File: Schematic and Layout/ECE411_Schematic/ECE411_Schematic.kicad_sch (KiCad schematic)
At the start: 17 parts, among them J1 Raspberry Pi GPIO, J2 AudioJack3, M1 Motor_DC, U1 CAT24C256, U2 PCF8574, U3 LM386, U4 L293D Driver

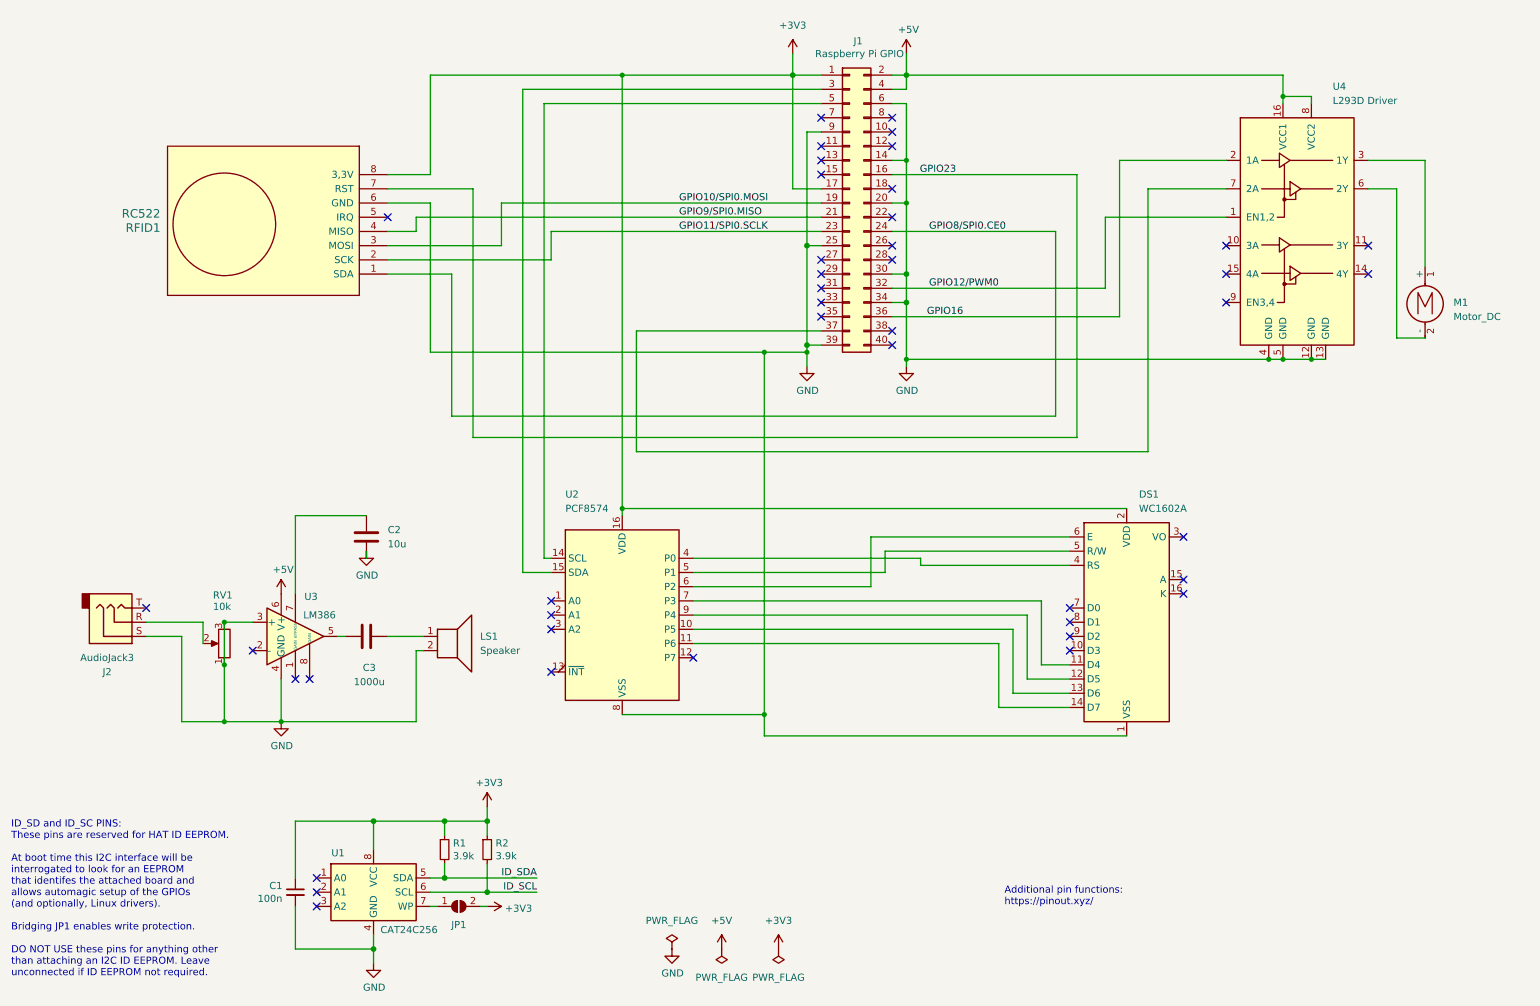
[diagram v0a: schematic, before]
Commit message: added LEDs to indicate functioning subsystems
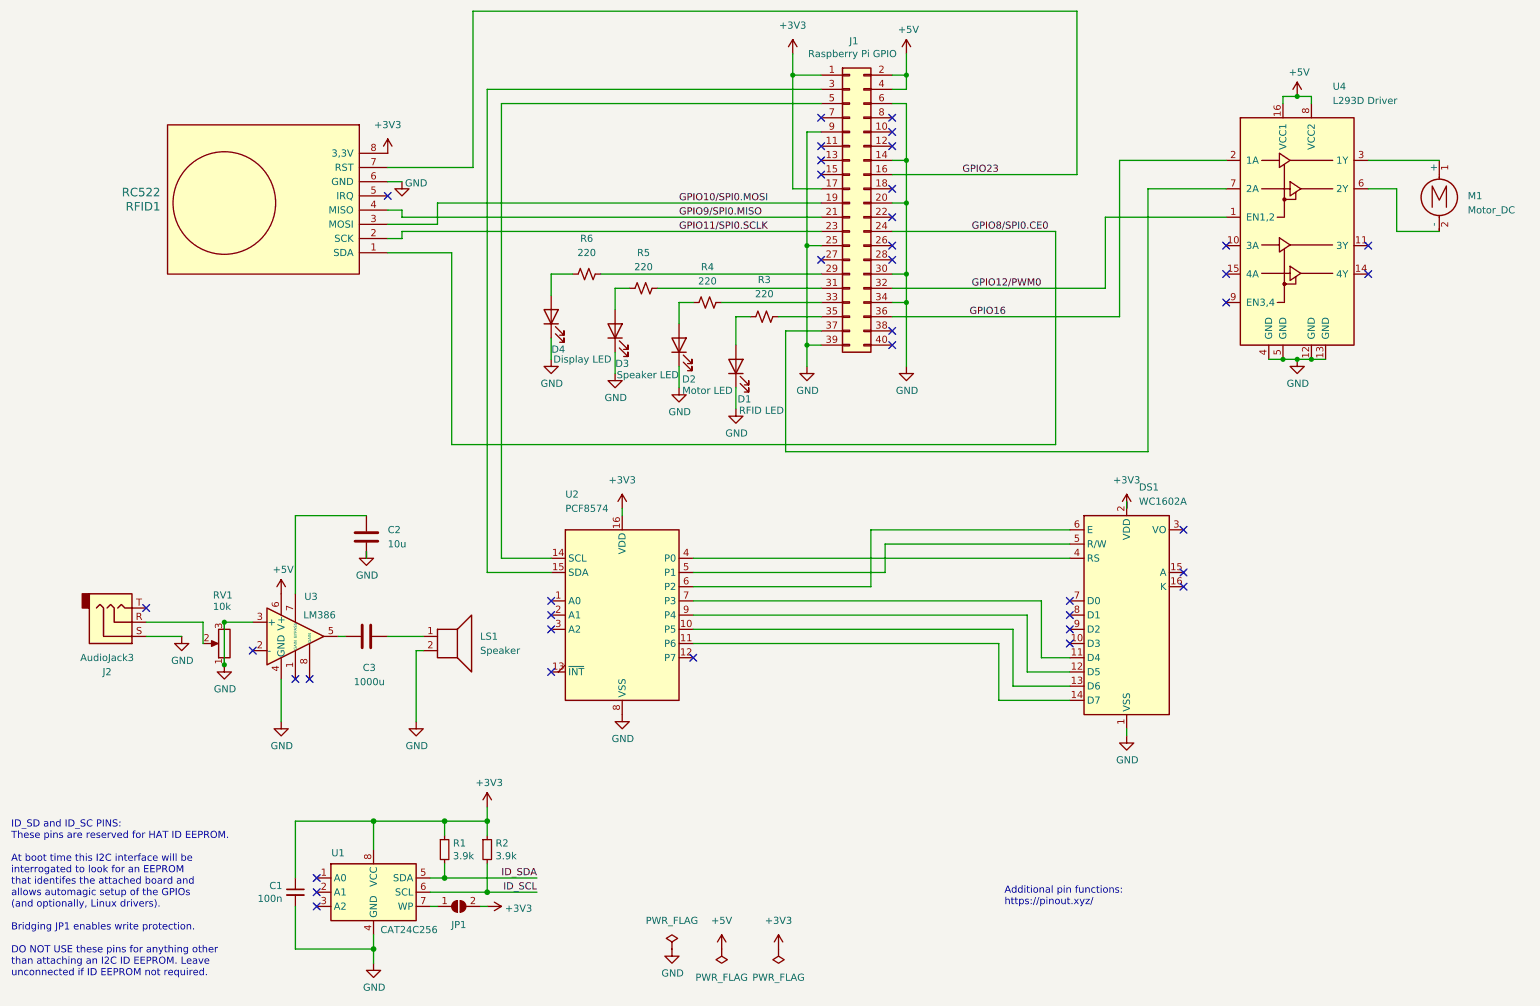
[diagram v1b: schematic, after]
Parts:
- added D1: RFID LED, LED_THT:LED_D5.0mm, symbol Device:LED
- added D2: Motor LED, LED_THT:LED_D5.0mm, symbol Device:LED
- added D3: Speaker LED, LED_THT:LED_D5.0mm, symbol Device:LED
- added D4: Display LED, LED_THT:LED_D5.0mm, symbol Device:LED
- added R3, R4, R5, R6: 220, Resistor_THT:R_Axial_DIN0204_L3.6mm_D1.6mm_P7.62mm_Horizontal, symbol Device:R_Small_US
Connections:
- net GND: now also D1.1 (K), D2.1 (K), D3.1 (K), D4.1 (K)
- net at J1.29 (Pin_29): now also R6.2
- net at J1.31 (Pin_31): now also R5.2
- net at J1.33 (Pin_33): now also R4.2
- net at J1.35 (Pin_35): now also R3.2
- new net: D1.2 (A), R3.1
- new net: D4.2 (A), R6.1
- new net: D3.2 (A), R5.1
- new net: D2.2 (A), R4.1
- no-connect marks 43 -> 39
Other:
- moved on the sheet: DS1, M1, RFID1
